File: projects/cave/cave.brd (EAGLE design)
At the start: 99 x 72 mm, 116 parts, among them U1 IRLML6344TRPBF, U10 IRLML6344TRPBF, U11 IRLML6344TRPBF, U12 IRLML6344TRPBF, U2 TLC555CDR, U3 IRLML6344TRPBF, U4 IRLML6344TRPBF, U5 IRLML6344TRPBF, U6 IRLML6344TRPBF, U7 TPS54625, U9 IRLML6344TRPBF

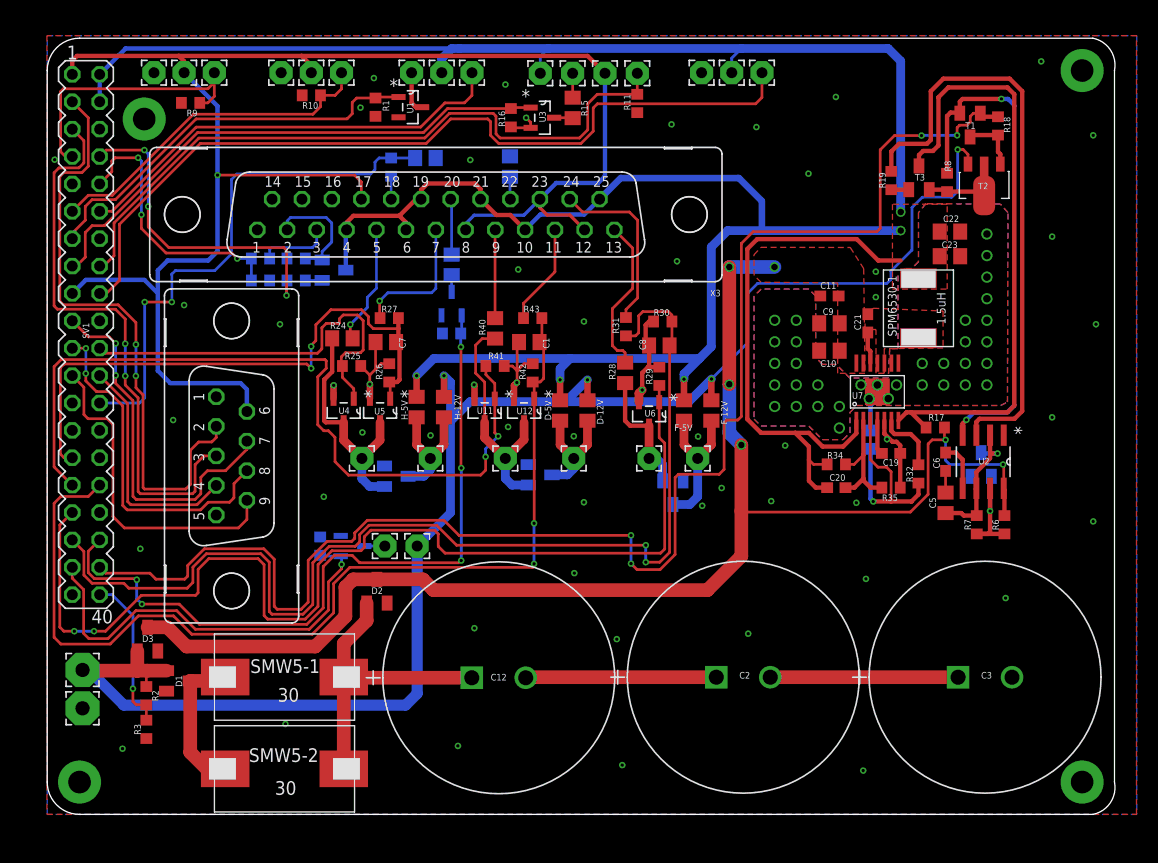
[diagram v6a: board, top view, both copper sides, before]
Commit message: MAJOR MODIFICATIONS: Changed power capacitor : previous ones didn't sustain discharge current Changed 555 capacitor : previous one was at 6.3V max (instead of 12V), AND not accurate enough -> switch to tantale capa Modified light_sensor circuit to use a phototransistor. The potentiometer is for schematic purpose, the package is NOT right !
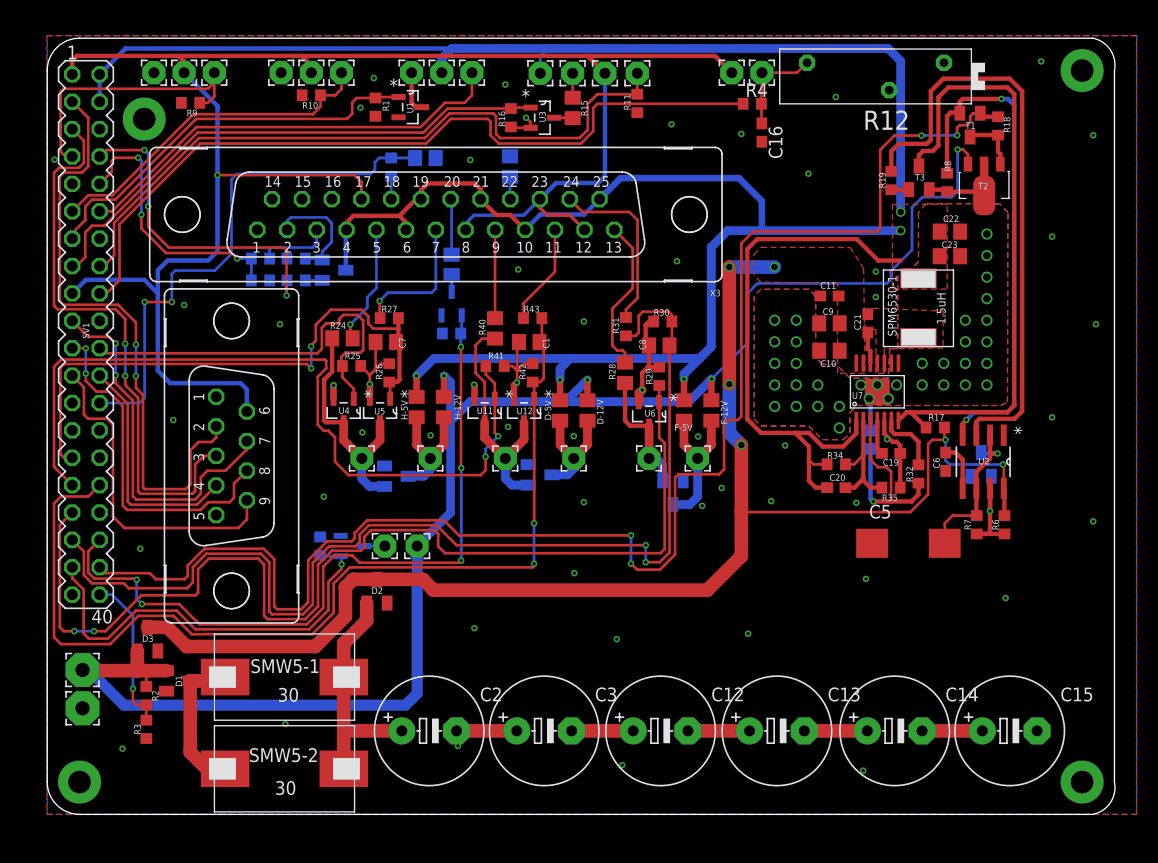
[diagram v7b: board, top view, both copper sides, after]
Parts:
- removed LIGHTSEN_GND: WIREPAD2,15/1,0, wirepad:2,15/1,0
- added C13, C14, C15: 4.7F/2.5V, rcl:E5-10,5
- added C16: 0.1uF/25V, rcl:C0603
- added R12: 5k, rcl:PT-SPIN
- added R4: 100, rcl:R0603
- C12, C2, C3: value 0.47F -> 4.7F/2.5V; device Panasonic-EEC-EECR-EECF-EECS:CAP_EECF5 -> rcl:E5-10,5
- C5: value 100uF/6.3V -> 100uF/16V; device rcl:C0805 -> resistor:D/7343-31W
- R1, R11, R16, R25, R26, R29, R30, R39, R41, R42: value 100k -> 10k
- moved C3 43.7 mm to (46.1, 7.75)
- moved C2 32.0 mm to (35.4, 7.75)
- moved C12 13.4 mm to (56.9, 7.75)
- moved C5 5.10 mm to (79.9, 25.1), turned to 0 degrees
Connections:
- new net N$18: C13.-, C14.+
- new net N$19: C14.-, C15.+
- new net N$21: C16.1, LIGHTSEN_SIG.1, R12.2, R4.2
- new net N$8: C12.-, C13.+
- net +3V3: now also LIGHTSEN_5V.1
- net +5V: no longer LIGHTSEN_5V.1
- net GND: now also C15.-, C16.2, C5.-, R12.3; no longer C3.2, C5.2, LIGHTSEN_GND.1
- net LIGHT_SENSOR: now also R4.1; no longer LIGHTSEN_SIG.1
- net N$1: now also C2.+; no longer C12.1
- net N$2: now also C2.-, C3.+; no longer C12.2, C2.1
- net N$3: now also C12.+, C3.-; no longer C2.2, C3.1
- net N$6: now also C5.+; no longer C5.1
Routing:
- net +3V3: track 154.5 -> 168.5 mm
- net N$2: track 17.7 -> 5.59 mm
- net N$3: track 17.4 -> 5.72 mm
- net N$21: track 0.00 -> 9.31 mm
- net N$1: track 28.2 -> 21.7 mm
- net N$18: track 0.00 -> 5.84 mm
- net N$8: track 0.00 -> 5.71 mm
- net N$19: track 0.00 -> 5.59 mm
- net LIGHT_SENSOR: track 78.2 -> 73.9 mm
- net +5V: track 274.8 -> 272.2 mm
- net N$6: track 13.3 -> 15.5 mm
- net GND: track 49.5 -> 47.5 mm

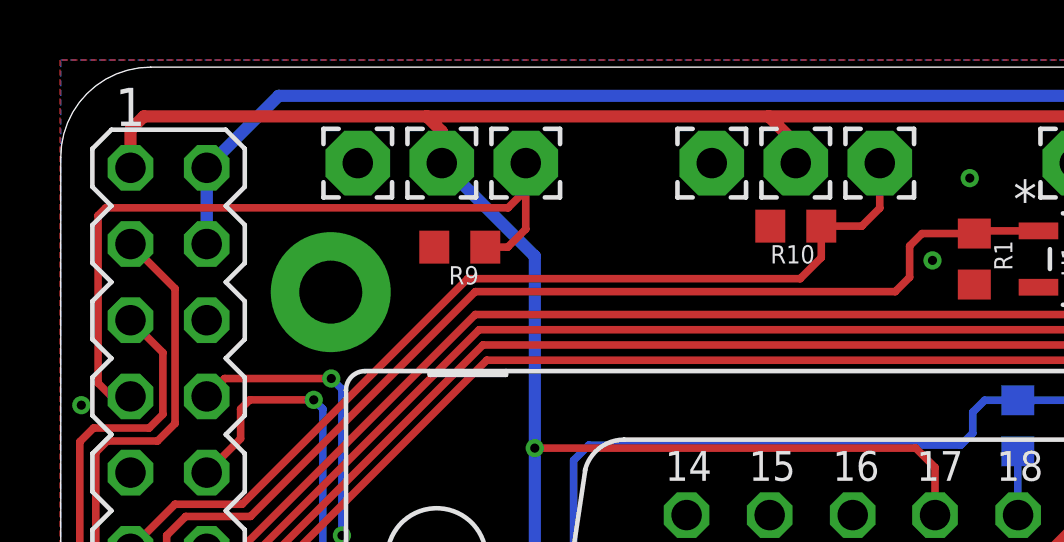
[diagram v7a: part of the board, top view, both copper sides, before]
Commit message: DHT22 circuit : the 4.7kOhm resistor change to pullup instead of pulldown (pulldown NOT working). Now DHT22 readings work fine.
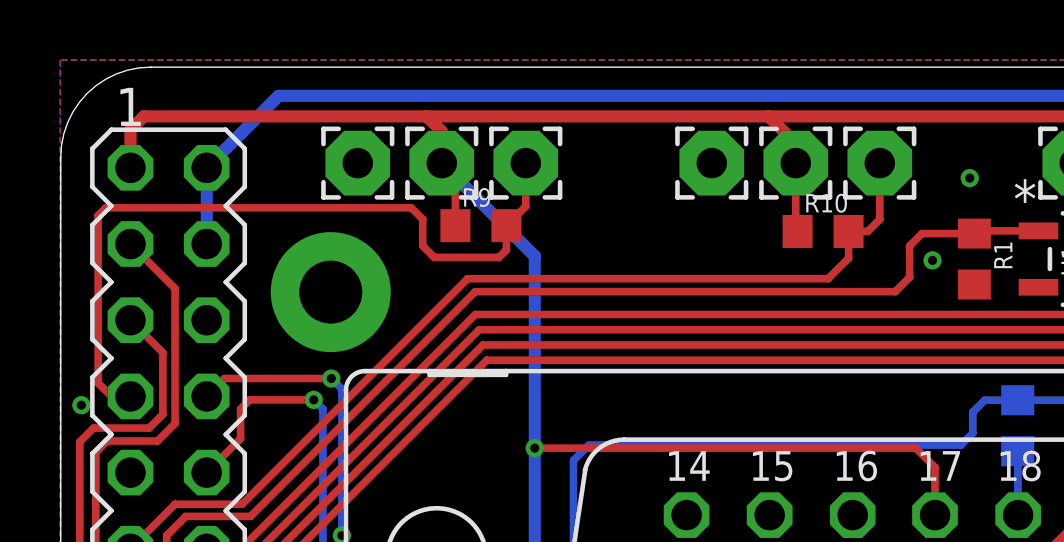
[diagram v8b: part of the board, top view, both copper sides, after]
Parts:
- moved R9 1.00 mm to (14.0, 66.7), turned to 0 degrees
- moved R10 0.93 mm to (25.4, 66.5), turned to 0 degrees
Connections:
- net +3V3: now also R10.1, R9.1
- net DHT22_EXT: now also R10.2; no longer R10.1
- net DHT22_INT: now also R9.2; no longer R9.1
- net GND: no longer R10.2, R9.2
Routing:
- net +3V3: track 168.5 -> 173.1 mm
- net DHT22_INT: track 26.2 -> 25.0 mm
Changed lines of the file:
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@@
 <attribute name="VALUE" x="32.3576" y="64.967" size="0.6096" layer="27" rot="R90"/>
 </element>
-<element name="R10" library="rcl" package="R0603" value="4.7k" x="24.5" y="66.7" smashed="yes" rot="R180">
-<attribute name="NAME" x="25.135" y="66.065" size="0.6096" layer="25" rot="R180"/>
-<attribute name="VALUE" x="25.135" y="68.605" size="0.6096" layer="27" rot="R180"/>
+<element name="R10" library="rcl" package="R0603" value="4.7k" x="25.411" y="66.523" smashed="yes">
+<attribute name="NAME" x="24.776" y="67.158" size="0.6096" layer="25"/>
+<attribute name="VALUE" x="24.776" y="64.618" size="0.6096" layer="27"/>
 </element>
 <element name="R11" library="rcl" package="R0603" value="10k" x="54.7306" y="65.945" smashed="yes" rot="R90">
@@
 <attribute name="VALUE" x="85.3749" y="57.984" size="0.6096" layer="27" rot="R90"/>
 </element>
-<element name="R9" library="rcl" package="R0603" value="4.7k" x="13.3" y="66" smashed="yes" rot="R180">
-<attribute name="NAME" x="13.935" y="65.365" size="0.6096" layer="25" rot="R180"/>
-<attribute name="VALUE" x="14.607" y="68.22" size="0.6096" layer="27" rot="R180"/>
+<element name="R9" library="rcl" package="R0603" value="4.7k" x="14.005" y="66.715" smashed="yes">
+<attribute name="NAME" x="13.37" y="67.35" size="0.6096" layer="25"/>
+<attribute name="VALUE" x="12.698" y="64.495" size="0.6096" layer="27"/>
 </element>
 <element name="SERVO_5V" library="wirepad" package="2,15/1,0" value="WIREPAD2,15/1,0" x="36.6" y="68.8" smashed="yes">
@@
 <contactref element="R29" pad="2"/>
 <contactref element="DHT-INT_GND" pad="1"/>
-<contactref element="R9" pad="2"/>
 <contactref element="DHT-EXT_GND" pad="1"/>
-<contactref element="R10" pad="2"/>
 <contactref element="R11" pad="1"/>
 <contactref element="U3" pad="2"/>
@@
 <contactref element="SV1" pad="11"/>
 <contactref element="DHT-EXT_SIG" pad="1"/>
-<contactref element="R10" pad="1"/>
 <wire x1="13.5636" y1="64.9478" x2="6.0452" y2="57.4294" width="0.254" layer="1"/>
 <wire x1="6.0452" y1="57.4294" x2="3.81" y2="57.4294" width="0.254" layer="1"/>
 <wire x1="3.81" y1="57.4294" x2="2.3241" y2="55.9435" width="0.254" layer="1"/>
-<wire x1="25.35" y1="66.7" x2="26.7" y2="66.7" width="0.254" layer="1"/>
-<wire x1="26.7" y1="66.7" x2="27.3" y2="67.3" width="0.254" layer="1"/>
-<wire x1="27.3" y1="67.3" x2="27.3" y2="68.8" width="0.254" layer="1"/>
-<wire x1="25.35" y1="66.7" x2="25.35" y2="65.65" width="0.254" layer="1"/>
-<wire x1="25.35" y1="65.65" x2="24.6478" y2="64.9478" width="0.254" layer="1"/>
-<wire x1="24.6478" y1="64.9478" x2="13.5636" y2="64.9478" width="0.254" layer="1"/>
+<wire x1="25.5778" y1="64.9478" x2="13.5636" y2="64.9478" width="0.254" layer="1"/>
+<contactref element="R10" pad="2"/>
+<wire x1="25.5778" y1="64.9478" x2="26.261" y2="65.631" width="0.254" layer="1"/>
+<wire x1="26.261" y1="65.631" x2="26.261" y2="66.523" width="0.254" layer="1"/>
+<wire x1="26.261" y1="66.523" x2="26.899" y2="66.523" width="0.254" layer="1"/>
+<wire x1="26.899" y1="66.523" x2="27.3" y2="66.924" width="0.254" layer="1"/>
+<wire x1="27.3" y1="66.924" x2="27.3" y2="68.8" width="0.254" layer="1"/>
 </signal>
 <signal name="SERVO_ON/OFF">
@@
 <wire x1="50.1246" y1="70.358" x2="61.942" y2="70.358" width="0.4064" layer="1"/>
 <wire x1="61.942" y1="70.358" x2="63.5" y2="68.8" width="0.4064" layer="1"/>
+<contactref element="R9" pad="1"/>
+<contactref element="R10" pad="1"/>
+<wire x1="24.561" y1="66.523" x2="24.5" y2="66.584" width="0.254" layer="1"/>
+<wire x1="24.5" y1="66.584" x2="24.5" y2="68.8" width="0.254" layer="1"/>
+<wire x1="13.155" y1="66.715" x2="13.155" y2="68.345" width="0.254" layer="1"/>
+<wire x1="13.155" y1="68.345" x2="12.7" y2="68.8" width="0.254" layer="1"/>
 </signal>
 <signal name="I2C_SDA">
@@
 <contactref element="SV1" pad="7"/>
 <contactref element="DHT-INT_SIG" pad="1"/>
-<contactref element="R9" pad="1"/>
 <wire x1="1.4986" y1="67.31" x2="1.2446" y2="67.056" width="0.254" layer="1"/>
 <wire x1="1.2446" y1="67.056" x2="1.2446" y2="61.468" width="0.254" layer="1"/>
 <wire x1="1.2446" y1="61.468" x2="1.6891" y2="61.0235" width="0.254" layer="1"/>
 <wire x1="1.6891" y1="61.0235" x2="2.3241" y2="61.0235" width="0.254" layer="1"/>
-<wire x1="14.15" y1="66" x2="14.9" y2="66" width="0.254" layer="1"/>
-<wire x1="14.9" y1="66" x2="15.5" y2="66.6" width="0.254" layer="1"/>
-<wire x1="15.5" y1="66.6" x2="15.5" y2="68.8" width="0.254" layer="1"/>
-<wire x1="15.5" y1="68.8" x2="15.5" y2="67.9" width="0.254" layer="1"/>
-<wire x1="15.5" y1="67.9" x2="14.91" y2="67.31" width="0.254" layer="1"/>
-<wire x1="14.91" y1="67.31" x2="1.4986" y2="67.31" width="0.254" layer="1"/>
+<contactref element="R9" pad="2"/>
+<wire x1="14.855" y1="66.715" x2="15.5" y2="67.36" width="0.254" layer="1"/>
+<wire x1="15.5" y1="67.36" x2="15.5" y2="68.8" width="0.254" layer="1"/>
+<wire x1="14.855" y1="66.715" x2="14.855" y2="65.909" width="0.254" layer="1"/>
+<wire x1="14.855" y1="65.909" x2="14.605" y2="65.659" width="0.254" layer="1"/>
+<wire x1="14.605" y1="65.659" x2="12.446" y2="65.659" width="0.254" layer="1"/>
+<wire x1="12.446" y1="65.659" x2="12.065" y2="66.04" width="0.254" layer="1"/>
+<wire x1="12.065" y1="66.04" x2="12.065" y2="66.929" width="0.254" layer="1"/>
+<wire x1="12.065" y1="66.929" x2="11.684" y2="67.31" width="0.254" layer="1"/>
+<wire x1="11.684" y1="67.31" x2="1.4986" y2="67.31" width="0.254" layer="1"/>
 </signal>
 <signal name="UART_RX_5V">
